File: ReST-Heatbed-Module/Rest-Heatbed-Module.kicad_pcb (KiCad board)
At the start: 2 copper layers, 30.4 x 47.8 mm, 16 parts, among them P1 02-SCREW-TERM, P2 02X04-MALE, P3 02-SCREW-TERM, P4 01X02-MALE, P5 02-SCREW-TERM, Q1 Q_BSH105, Q2 Q_AOT240L

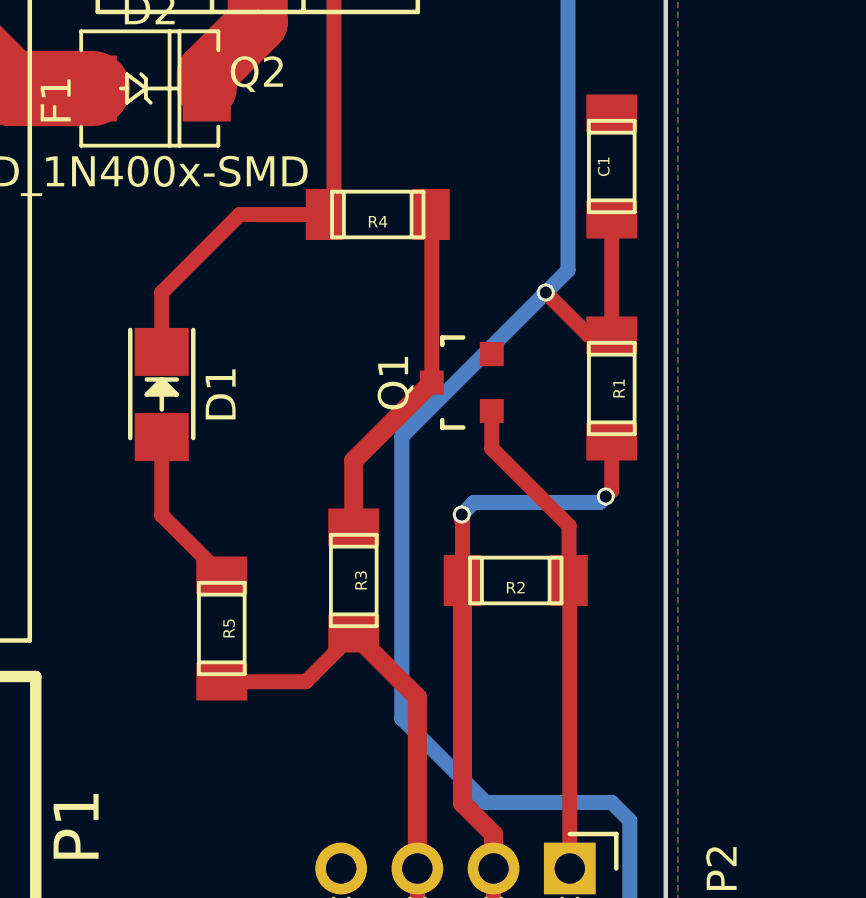
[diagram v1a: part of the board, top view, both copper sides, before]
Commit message: PRE-RELEASE Rev. A!
Yay. I managed to finish the Main PCB over the night, must say, Im happy with it. Things that changed since the last release:

Heater:
-Heater Module uses less Pins
- Much smaller Design now

Heatbed & Additional Module: 
-Changed distance from Edge to first Pin from 2.5mm to 2mm (will be changed on other boards too)

Mainboard:
-Added I2C Pullups 4K7
-Swapped Pins from Stepper, Heaters and Endstops around for easier PCB Design.
-Finished Design (10cm x 10cm!)

Added some 3D Models for testing. If someone has problems with loading some modules, please contact me! (or make a pull request with a better solution)
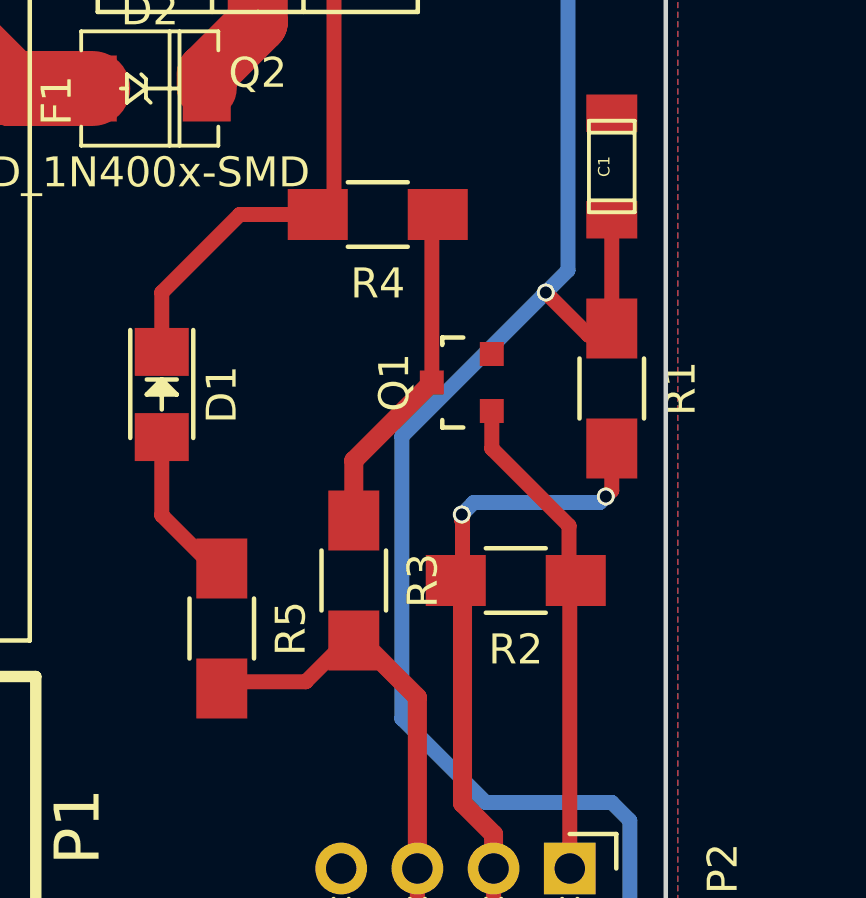
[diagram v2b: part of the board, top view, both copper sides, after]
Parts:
- R1, R2, R3, R4, R5: footprint ok-smd-generic:1206 -> Resistors_SMD:R_1206_HandSoldering

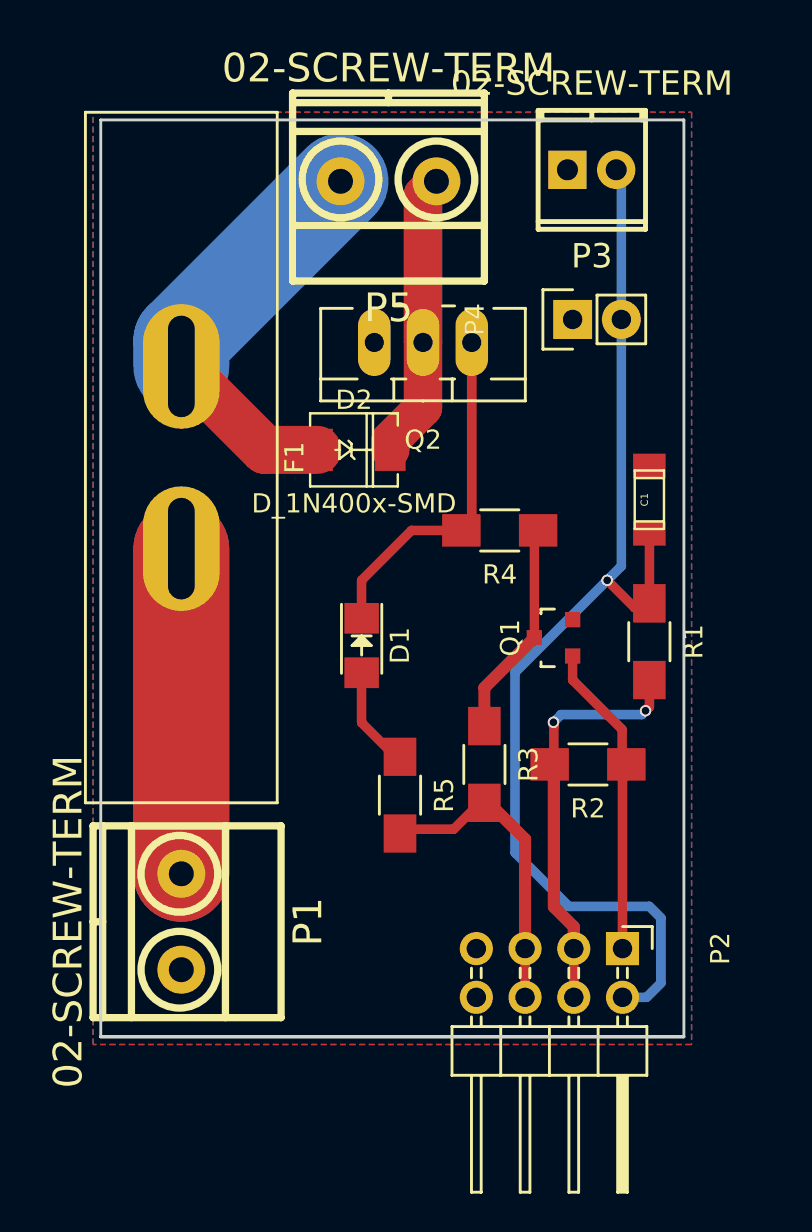
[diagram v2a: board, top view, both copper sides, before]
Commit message: Added Images and PDF's
+ Silkscreening
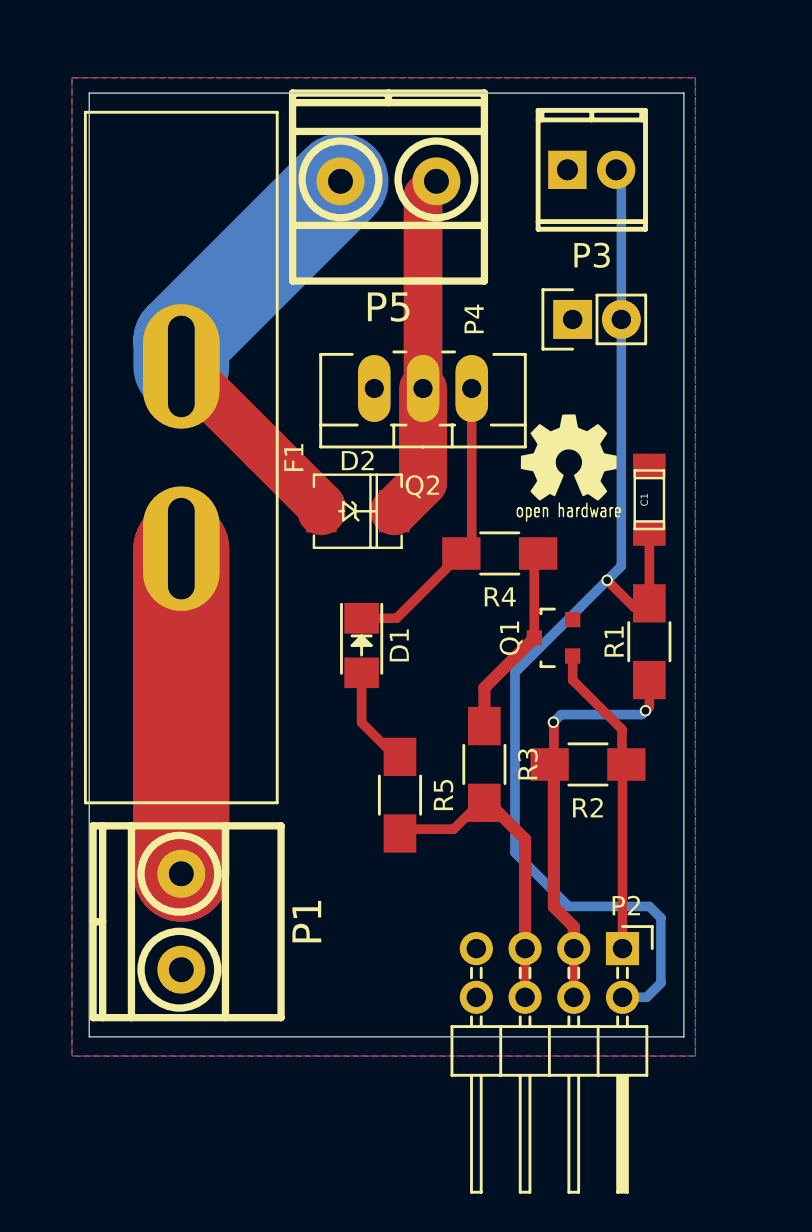
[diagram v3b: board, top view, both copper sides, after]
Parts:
- added G***: LOGO, ReST-Library:Logo_silk_OSHW_6x6mm, F.Cu at (137.2, 124.4)
- added G***: LOGO, ReST-Library:STM32, B.Cu at (130.0, 144.4)
- moved D2 3.21 mm to (126.2, 127.2)
- moved Q2 2.40 mm to (129.6, 120.8)
- moved R4 1.20 mm to (133.6, 129.4)
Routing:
- net Net-(D2-Pad2): track 23.7 -> 29.2 mm
- net Net-(D1-Pad1): track 18.9 -> 15.4 mm
- net +12V: track 22.0 -> 23.7 mm
- net Net-(Q1-Pad3): track 11.5 -> 10.4 mm
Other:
- board size 30.4 x 47.8 mm -> 31 x 49.2 mm
- board text added: "ReST32 Heatbed Module Rev. A | Test"
- board text added: "by Straw"

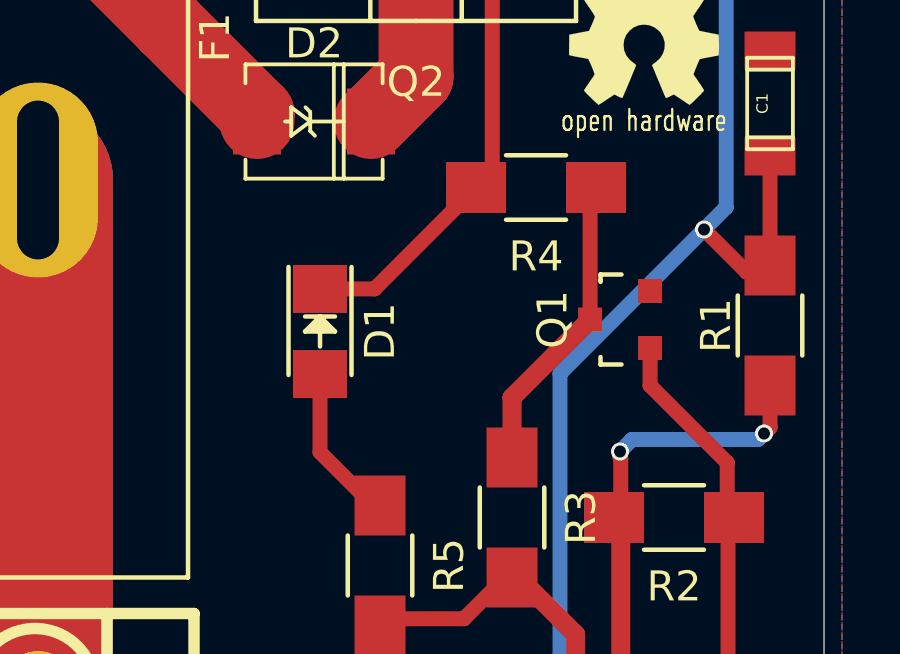
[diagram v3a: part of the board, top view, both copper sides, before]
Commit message: Added Mounting Holes to all Modules
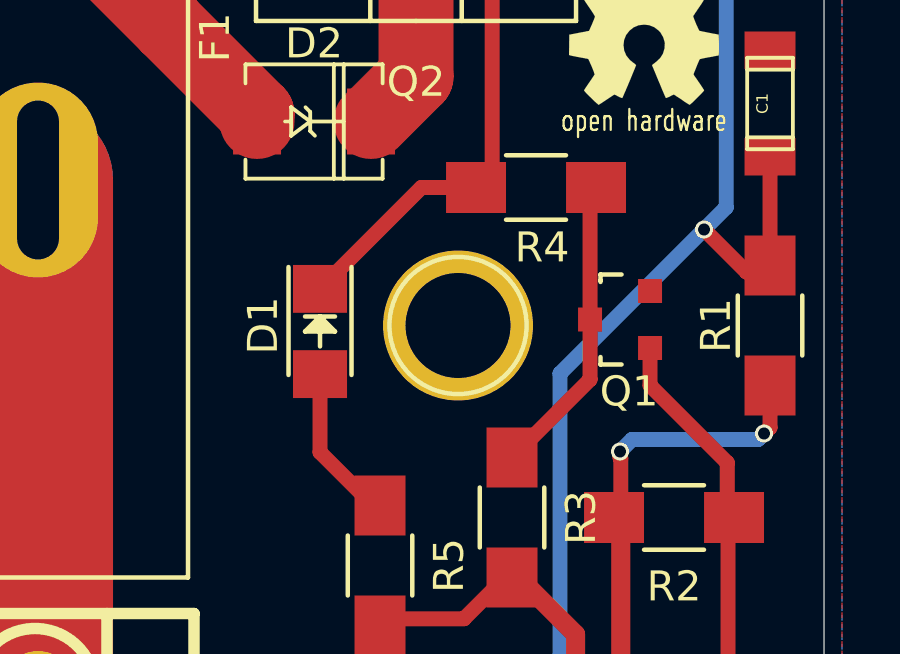
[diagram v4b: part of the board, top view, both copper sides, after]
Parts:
- added ?: 1pin, Connect:1pin, F.Cu at (131.0, 134.0)
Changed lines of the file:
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@@
     (links 29)
     (no_connects 0)
-    (area 109.4 102.4 148.803543 163.425001)
+    (area 112.194999 105.394999 143.205001 154.605001)
     (thickness 1.6)
     (drawings 6)
     (tracks 69)
     (zones 0)
-    (modules 18)
+    (modules 19)
     (nets 12)
   )
@@
   )
   (setup
-    (last_trace_width 0.25)
+    (last_trace_width 0.5)
     (user_trace_width 0.5)
     (user_trace_width 2)
@@
     (mod_text_size 1 1)
     (mod_text_width 0.15)
-    (pad_size 1.524 1.524)
-    (pad_drill 0.762)
+    (pad_size 5 5)
+    (pad_drill 3.5)
     (pad_to_mask_clearance 0.2)
     (aux_axis_origin 0 0)
@@
     (tags "LED1206 SMD")
     (attr smd)
-    (fp_text reference D1 (at 0 -2 270) (layer F.SilkS)
+    (fp_text reference D1 (at -0.2 1.9 270) (layer F.SilkS)
       (effects (font (size 1 1) (thickness 0.15)))
     )
@@
     (tags SOT-23)
     (attr smd)
-    (fp_text reference Q1 (at 0 -2.25 90) (layer F.SilkS)
+    (fp_text reference Q1 (at -2.4 0.3 180) (layer F.SilkS)
       (effects (font (size 1 1) (thickness 0.15)))
     )
@@
     (tags "resistor 1206")
     (attr smd)
-    (fp_text reference R4 (at 0 -2.3 180) (layer F.SilkS)
+    (fp_text reference R4 (at -0.2 -2 180) (layer F.SilkS)
       (effects (font (size 1 1) (thickness 0.15)))
     )
@@
       (xy -1.561828 2.12361) (xy -1.438134 2.119828)) (layer B.SilkS) (width 0.01))
   )
-  (gr_text "by Straw" (at 129.4 140.6) (layer B.SilkS)
+  (module Connect:1pin (layer F.Cu)
+    (at 131 134)
+    (descr "module 1 pin (ou trou mecanique de percage)")
+    (tags DEV)
+    (fp_text reference "" (at 0 -3.048) (layer F.SilkS) hide
+      (effects (font (size 1 1) (thickness 0.15)))
+    )
+    (fp_text value 1pin (at 0 2.794) (layer F.Fab)
+      (effects (font (size 1 1) (thickness 0.15)))
+    )
+    (fp_circle (center 0 0) (end 0 -2.286) (layer F.SilkS) (width 0.15))
+    (pad 1 thru_hole circle (at 0 0) (size 5 5) (drill 3.5) (layers *.Cu *.Mask F.SilkS))
+  )
+  (gr_text "by Straw" (at 129.5 138.2) (layer B.SilkS)
     (effects (font (size 1 1) (thickness 0.2)) (justify mirror))
   )
-  (gr_text "ReST32 Heatbed Module\nRev. A | Test" (at 128.4 136.4) (layer B.SilkS)
+  (gr_text "ReST32 Heatbed Module\nRev. A | Test" (at 129.2 125.5) (layer B.SilkS)
     (effects (font (size 1.5 1.5) (thickness 0.2)) (justify mirror))
   )
@@
   (segment (start 126.4 135.61986) (end 126.4 138.22454) (width 0.5) (layer F.Cu) (net 3))
   (segment (start 126.4 138.22454) (end 128.4 140.22454) (width 0.5) (layer F.Cu) (net 3))
+  (segment (start 131.6 129.4) (end 129.78014 129.4) (width 0.5) (layer F.Cu) (net 4))
+  (segment (start 129.78014 129.4) (end 126.4 132.78014) (width 0.5) (layer F.Cu) (net 4))
   (segment (start 131.6 129.4) (end 132.14 128.86) (width 0.5) (layer F.Cu) (net 4))
   (segment (start 132.14 128.86) (end 132.14 120.8) (width 0.5) (layer F.Cu) (net 4))
-  (segment (start 126.4 132.78014) (end 128.21986 132.78014) (width 0.5) (layer F.Cu) (net 4))
-  (segment (start 128.21986 132.78014) (end 131.6 129.4) (width 0.5) (layer F.Cu) (net 4))
   (segment (start 124.30008 127.2) (end 124.30008 126.95008) (width 2.5) (layer F.Cu) (net 5))
   (segment (start 124.30008 126.95008) (end 121.35 124) (width 2.5) (layer F.Cu) (net 5))
@@
   (segment (start 140 140.42454) (end 139.97546 140.4) (width 0.635) (layer F.Cu) (net 10))
   (segment (start 140 140.42454) (end 139.97546 140.4) (width 0.25) (layer F.Cu) (net 10))
+  (segment (start 135.40178 133.8) (end 135.40178 135.79822) (width 0.5) (layer F.Cu) (net 11))
+  (segment (start 135.40178 135.79822) (end 132.8 138.4) (width 0.5) (layer F.Cu) (net 11))
   (segment (start 135.40178 133.8) (end 135.40178 129.59822) (width 0.5) (layer F.Cu) (net 11))
   (segment (start 135.40178 129.59822) (end 135.6 129.4) (width 0.5) (layer F.Cu) (net 11))
   (segment (start 135.40178 129.42632) (end 135.37546 129.4) (width 0.5) (layer F.Cu) (net 11) (status 30))
-  (segment (start 132.8 138.62454) (end 132.8 136.40178) (width 0.635) (layer F.Cu) (net 11))
-  (segment (start 132.8 136.40178) (end 135.40178 133.8) (width 0.635) (layer F.Cu) (net 11))
   (zone (net 2) (net_name GND) (layer F.Cu) (hatch edge 0.508)
     (connect_pads (clearance 0.5))
